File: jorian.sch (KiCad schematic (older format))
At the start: 101 parts, among them J1 USB-C, J2 USB-C, J3 MicroUSB, J4 MicroUSB, J5 MJ-4PP-9, Q1 AO3407, SW1 MSK-12C02, U1 E73-2G4M08S1C-52840, U2 E73-2G4M08S1C-52840, U3 MCP73831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

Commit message: updated files
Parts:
- removed H1: Battery Pad, kbd:battery_pad, symbol Mechanical:MountingHole_Pad
- removed JP1: +, kbd:jumper, symbol Device:Jumper_NO_Small
- removed JP10: -, kbd:jumper, symbol Device:Jumper_NO_Small
- removed JP16, JP25, JP26, JP27, JP28, JP29, JP30, JP31: (no value), kbd:jumper, symbol Device:Jumper_NO_Small
- removed OLED2: I2C_conn, kbd:connector_i2c, symbol Connector_Generic:Conn_01x04
- added Q2: SI2306, Package_TO_SOT_SMD:SOT-23, symbol Transistor_FET:BS870
- added R3: 10K, Resistor_SMD:R_0603_1608Metric, symbol Device:R
- JP11: symbol Connector_Generic:Conn_01x04 -> Connector_Generic:Conn_01x02
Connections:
- net labels added: LED_GND
- net labels removed: PGND
- wire segments 334 -> 317
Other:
- note added: "Power Control\nNormally On\nLow - Off\n"
- moved on the sheet: J5, U1, U2, X1

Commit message: updated files
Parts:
- removed J3, J4: MicroUSB, kbd:usb_micro_custom, symbol Connector:USB_B_Micro
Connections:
- no-connect marks 18 -> 14
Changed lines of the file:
@@
 	8000 9300 8500 9300
-$Comp
-L Connector:USB_B_Micro J3
-U 1 1 5DDAA442
-P 13125 5500
-F 0 "J3" H 13180 5967 50  0000 C CNN
-F 1 "MicroUSB" H 13180 5876 50  0000 C CNN
-F 2 "kbd:usb_micro_custom" H 13275 5450 50  0001 C CNN
-F 3 "~" H 13275 5450 50  0001 C CNN
-	1    13125 5500
-	1    0    0    -1
-$EndComp
-Text Label 13425 5300 0    50   ~ 0
-VUSB
-NoConn ~ 13025 5900
 $Comp
 L power:GND #PWR0108
@@
 Wire Wire Line
 	15125 5525 15125 5575
-NoConn ~ 13000 7125
-NoConn ~ 13400 6925
 NoConn ~ 14225 6525
 NoConn ~ 15125 6225
@@
 NoConn ~ 15125 5325
 NoConn ~ 15125 5225
-Text Label 13400 6525 0    50   ~ 0
-VUSB
-$Comp
-L Connector:USB_B_Micro J4
-U 1 1 5DDAA45A
-P 13100 6725
-F 0 "J4" H 13155 7192 50  0000 C CNN
-F 1 "MicroUSB" H 13155 7101 50  0000 C CNN
-F 2 "kbd:usb_micro_custom" H 13250 6675 50  0001 C CNN
-F 3 "~" H 13250 6675 50  0001 C CNN
-	1    13100 6725
-	1    0    0    -1
-$EndComp
 $Comp
 L jorian-rescue:USB_C_Receptacle_USB2.0-Connector J1
@@
 	1    0    0    -1
 $EndComp
-NoConn ~ 13425 5700
-$Comp
-L power:GND #PWR0109
-U 1 1 5DDAA46D
-P 13125 5900
-F 0 "#PWR0109" H 13125 5650 50  0001 C CNN
-F 1 "GND" H 13125 5750 50  0000 C CNN
-F 2 "" H 13125 5900 50  0001 C CNN
-F 3 "" H 13125 5900 50  0001 C CNN
-	1    13125 5900
-	-1   0    0    -1
-$EndComp
-$Comp
-L power:GND #PWR0112
-U 1 1 5DDAA473
-P 13100 7125
-F 0 "#PWR0112" H 13100 6875 50  0001 C CNN
-F 1 "GND" H 13100 6975 50  0000 C CNN
-F 2 "" H 13100 7125 50  0001 C CNN
-F 3 "" H 13100 7125 50  0001 C CNN
-	1    13100 7125
-	-1   0    0    -1
-$EndComp
 Text GLabel 15225 5575 2    50   Input ~ 0
 D-
@@
 Wire Wire Line
 	15125 5775 15225 5775
-Text GLabel 13425 5500 2    50   Input ~ 0
-D+
-Text GLabel 13425 5600 2    50   Input ~ 0
-D-
-Text GLabel 13400 6825 2    50   Input ~ 0
-D-
-Text GLabel 13400 6725 2    50   Input ~ 0
-D+
 Text GLabel 15125 5025 2    50   Input ~ 0
 VUSB

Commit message: updated files
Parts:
- removed JP18: LIPO+, kbd:jumper, symbol Device:Jumper_NO_Small
- removed JP19: LIPO-, kbd:jumper, symbol Device:Jumper_NO_Small
- removed JP20: BAT+, kbd:jumper, symbol Device:Jumper_NO_Small
- removed JP21: BAT-, kbd:jumper, symbol Device:Jumper_NO_Small
- added Q3: AO3407, Package_TO_SOT_SMD:SOT-23, symbol Transistor_FET:BSS83P
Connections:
- net labels added: LED_VCC
- net labels removed: LED_GND, LIPO+, LIPO-
- wire segments 317 -> 320
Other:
- moved on the sheet: BT1, C1, C2, C3, D1, D2, JP11, JP2, JP3, JP4, JP5, JP6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

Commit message: updated files
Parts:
- removed J2: USB-C, kbd:usb_type_c, symbol jorian-rescue:USB_C_Receptacle_USB2.0-Connector
- removed U2: E73-2G4M08S1C-52840, kbd:E73-2G4M08S1C-52840, symbol jorian-rescue:E73-2G4M08S1C-52840
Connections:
- net labels added: CC1, CC2
- wire segments 320 -> 303
- no-connect marks 14 -> 8
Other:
- moved on the sheet: R1, R2

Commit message: autorouted
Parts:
- removed JP11: SWD_conn, kbd:connector_swd, symbol Connector_Generic:Conn_01x02
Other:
- moved on the sheet: E10, E15, E16, E18, E19, E20, E21, E5, L18
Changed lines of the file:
@@
 L Connector_Generic:Conn_01x04 E16
 U 1 1 5C28A7CD
-P 10550 8100
-F 0 "E16" H 10550 8300 50  0000 C CNN
-F 1 "right" H 10550 7800 50  0000 C CNN
-F 2 "kbd:edge_conn" H 10550 8100 50  0001 C CNN
-F 3 "" H 10550 8100 50  0001 C CNN
-	1    10550 8100
+P 10300 7075
+F 0 "E16" H 10300 7275 50  0000 C CNN
+F 1 "right" H 10300 6775 50  0000 C CNN
+F 2 "kbd:edge_conn" H 10300 7075 50  0001 C CNN
+F 3 "" H 10300 7075 50  0001 C CNN
+	1    10300 7075
 	-1   0    0    -1
 $EndComp
@@
 L Connector_Generic:Conn_01x04 E18
 U 1 1 5C28AA80
-P 10350 8100
-F 0 "E18" H 10350 8300 50  0000 C CNN
-F 1 "left" H 10350 7800 50  0000 C CNN
-F 2 "kbd:edge_conn" H 10350 8100 50  0001 C CNN
-F 3 "" H 10350 8100 50  0001 C CNN
-	1    10350 8100
-	1    0    0    -1
-$EndComp
-Text Label 10750 8200 0    50   ~ 0
+P 10100 7075
+F 0 "E18" H 10100 7275 50  0000 C CNN
+F 1 "left" H 10100 6775 50  0000 C CNN
+F 2 "kbd:edge_conn" H 10100 7075 50  0001 C CNN
+F 3 "" H 10100 7075 50  0001 C CNN
+	1    10100 7075
+	1    0    0    -1
+$EndComp
+Text Label 10500 7175 0    50   ~ 0
 GND
-Text Label 10750 8300 0    50   ~ 0
+Text Label 10500 7275 0    50   ~ 0
 S18
-Text Label 10750 8000 0    50   ~ 0
+Text Label 10500 6975 0    50   ~ 0
 LED_VCC
 $Comp
 L Connector_Generic:Conn_01x04 E19
 U 1 1 5C6E087C
-P 10300 5250
-F 0 "E19" H 10300 5450 50  0000 C CNN
-F 1 "right" H 10300 4950 50  0000 C CNN
-F 2 "kbd:edge_conn" H 10300 5250 50  0001 C CNN
-F 3 "" H 10300 5250 50  0001 C CNN
-	1    10300 5250
+P 11800 5650
+F 0 "E19" H 11800 5850 50  0000 C CNN
+F 1 "right" H 11800 5350 50  0000 C CNN
+F 2 "kbd:edge_conn" H 11800 5650 50  0001 C CNN
+F 3 "" H 11800 5650 50  0001 C CNN
+	1    11800 5650
 	-1   0    0    -1
 $EndComp
@@
 L Connector_Generic:Conn_01x04 E5
 U 1 1 5C6E0883
-P 10100 5250
-F 0 "E5" H 10100 5450 50  0000 C CNN
-F 1 "left" H 10100 4950 50  0000 C CNN
-F 2 "kbd:edge_conn" H 10100 5250 50  0001 C CNN
-F 3 "" H 10100 5250 50  0001 C CNN
-	1    10100 5250
-	1    0    0    -1
-$EndComp
-Text Label 9900 5450 2    50   ~ 0
+P 11600 5650
+F 0 "E5" H 11600 5850 50  0000 C CNN
+F 1 "left" H 11600 5350 50  0000 C CNN
+F 2 "kbd:edge_conn" H 11600 5650 50  0001 C CNN
+F 3 "" H 11600 5650 50  0001 C CNN
+	1    11600 5650
+	1    0    0    -1
+$EndComp
+Text Label 11400 5850 2    50   ~ 0
 S19
-Text Label 9900 6150 2    50   ~ 0
+Text Label 11400 6550 2    50   ~ 0
 S20
 $Comp
 L Connector_Generic:Conn_01x04 E21
 U 1 1 5C6F2906
-P 10300 6650
-F 0 "E21" H 10300 6850 50  0000 C CNN
-F 1 "right" H 10300 6350 50  0000 C CNN
-F 2 "kbd:edge_conn" H 10300 6650 50  0001 C CNN
-F 3 "" H 10300 6650 50  0001 C CNN
-	1    10300 6650
+P 11800 7050
+F 0 "E21" H 11800 7250 50  0000 C CNN
+F 1 "right" H 11800 6750 50  0000 C CNN
+F 2 "kbd:edge_conn" H 11800 7050 50  0001 C CNN
+F 3 "" H 11800 7050 50  0001 C CNN
+	1    11800 7050
 	-1   0    0    -1
 $EndComp
@@
 L Connector_Generic:Conn_01x04 E15
 U 1 1 5C6F290D
-P 10100 6650
-F 0 "E15" H 10100 6850 50  0000 C CNN
-F 1 "left" H 10100 6350 50  0000 C CNN
-F 2 "kbd:edge_conn" H 10100 6650 50  0001 C CNN
-F 3 "" H 10100 6650 50  0001 C CNN
-	1    10100 6650
-	1    0    0    -1
-$EndComp
-Text Label 9900 5950 2    50   ~ 0
+P 11600 7050
+F 0 "E15" H 11600 7250 50  0000 C CNN
+F 1 "left" H 11600 6750 50  0000 C CNN
+F 2 "kbd:edge_conn" H 11600 7050 50  0001 C CNN
+F 3 "" H 11600 7050 50  0001 C CNN
+	1    11600 7050
+	1    0    0    -1
+$EndComp
+Text Label 11400 6350 2    50   ~ 0
 S22
-Text Label 10750 8100 0    50   ~ 0
+Text Label 10500 7075 0    50   ~ 0
 DIN18
-Text Label 10150 8300 2    50   ~ 0
+Text Label 9900 7275 2    50   ~ 0
 S18_A
-Text Label 10150 8200 2    50   ~ 0
+Text Label 9900 7175 2    50   ~ 0
 GND_A
-Text Label 10150 8000 2    50   ~ 0
+Text Label 9900 6975 2    50   ~ 0
 VCC_A
-Text Label 10150 8100 2    50   ~ 0
+Text Label 9900 7075 2    50   ~ 0
 DIN18_A
-Text Label 10500 5450 0    50   ~ 0
+Text Label 12000 5850 0    50   ~ 0
 S19_B
-Text Label 10500 6150 0    50   ~ 0
+Text Label 12000 6550 0    50   ~ 0
 S20_B
-Text Label 10500 6850 0    50   ~ 0
+Text Label 12000 7250 0    50   ~ 0
 S21_B
-Text Label 10500 5950 0    50   ~ 0
+Text Label 12000 6350 0    50   ~ 0
 S22_B
-Text Label 10500 6650 0    50   ~ 0
+Text Label 12000 7050 0    50   ~ 0
 VCC_B
-Text Label 10500 5250 0    50   ~ 0
+Text Label 12000 5650 0    50   ~ 0
 DIN21_B
-Text Label 9900 5150 2    50   ~ 0
+Text Label 11400 5550 2    50   ~ 0
 DIN5
-Text Label 10500 5150 0    50   ~ 0
+Text Label 12000 5550 0    50   ~ 0
 DIN5_B
-Text Label 9900 5250 2    50   ~ 0
+Text Label 11400 5650 2    50   ~ 0
 DIN21
 $Comp
@@
 L Connector_Generic:Conn_01x04 E20
 U 1 1 5C1C4E7E
-P 10300 5950
-F 0 "E20" H 10300 6150 50  0000 C CNN
-F 1 "right" H 10300 5650 50  0000 C CNN
-F 2 "kbd:edge_conn" H 10300 5950 50  0001 C CNN
-F 3 "" H 10300 5950 50  0001 C CNN
-	1    10300 5950
+P 11800 6350
+F 0 "E20" H 11800 6550 50  0000 C CNN
+F 1 "right" H 11800 6050 50  0000 C CNN
+F 2 "kbd:edge_conn" H 11800 6350 50  0001 C CNN
+F 3 "" H 11800 6350 50  0001 C CNN
+	1    11800 6350
 	-1   0    0    -1
 $EndComp
@@
 L Connector_Generic:Conn_01x04 E10
 U 1 1 5C1C4E85
-P 10100 5950
-F 0 "E10" H 10100 6150 50  0000 C CNN
-F 1 "left" H 10100 5650 50  0000 C CNN
-F 2 "kbd:edge_conn" H 10100 5950 50  0001 C CNN
-F 3 "" H 10100 5950 50  0001 C CNN
-	1    10100 5950
+P 11600 6350
+F 0 "E10" H 11600 6550 50  0000 C CNN
+F 1 "left" H 11600 6050 50  0000 C CNN
+F 2 "kbd:edge_conn" H 11600 6350 50  0001 C CNN
+F 3 "" H 11600 6350 50  0001 C CNN
+	1    11600 6350
 	1    0    0    -1
 $EndComp
@@
 L kbd:kbd_SK6812MINI L18
 U 1 1 5C54BB48
-P 9850 7375
-F 0 "L18" H 9850 7375 59  0000 C CNN
-F 1 "SK6812MINI" H 9850 7325 16  0000 C CNN
-F 2 "kbd:kbd_SK6812MINI" H 9850 7375 60  0001 C CNN
-F 3 "" H 9850 7375 60  0001 C CNN
-	1    9850 7375
+P 8175 7900
+F 0 "L18" H 8175 7900 59  0000 C CNN
+F 1 "SK6812MINI" H 8175 7850 16  0000 C CNN
+F 2 "kbd:kbd_SK6812MINI" H 8175 7900 60  0001 C CNN
+F 3 "" H 8175 7900 60  0001 C CNN
+	1    8175 7900
 	-1   0    0    -1
 $EndComp
-Text Label 9650 7275 2    50   ~ 0
+Text Label 7975 7800 2    50   ~ 0
 VCC_A
-Text Label 9650 7475 2    50   ~ 0
+Text Label 7975 8000 2    50   ~ 0
 DIN18_A
-Text Label 10050 7475 0    50   ~ 0
+Text Label 8375 8000 0    50   ~ 0
 GND_A
-NoConn ~ 10050 7275
+NoConn ~ 8375 7800
 Wire Wire Line
 	6100 3550 6100 4750
@@
 	0    -1   -1   0
 $EndComp
-Text GLabel 2500 1325 2    50   Input ~ 0
+Text GLabel 2500 2025 2    50   Input ~ 0
 S1
 $Comp
@@
 	1    0    0    -1
 $EndComp
-Text GLabel 2500 1225 2    50   Input ~ 0
+Text GLabel 2500 2125 2    50   Input ~ 0
 S2
-Text GLabel 2500 1125 2    50   Input ~ 0
+Text GLabel 2500 2225 2    50   Input ~ 0
 S3
 Text GLabel 1150 1925 0    50   Input ~ 0
@@
 Text GLabel 1150 1825 0    50   Input ~ 0
 S5
+Text GLabel 2500 1825 2    50   Input ~ 0
+S6
 Text GLabel 2500 1925 2    50   Input ~ 0
-S6
-Text GLabel 2500 1825 2    50   Input ~ 0
 S7
-Text GLabel 1150 2425 0    50   Input ~ 0
+Text GLabel 2500 2425 2    50   Input ~ 0
 S8
 Text GLabel 1150 1525 0    50   Input ~ 0
@@
 Text GLabel 1150 1325 0    50   Input ~ 0
 S10
-Text GLabel 1150 2625 0    50   Input ~ 0
+Text GLabel 2500 1425 2    50   Input ~ 0
 S11
-Text GLabel 2500 2025 2    50   Input ~ 0
+Text GLabel 2500 1625 2    50   Input ~ 0
 S12
 Text GLabel 1150 1025 0    50   Input ~ 0
 S13
-Text GLabel 2500 1425 2    50   Input ~ 0
+Text GLabel 1150 2625 0    50   Input ~ 0
 S14
-Text GLabel 2500 1625 2    50   Input ~ 0
+Text GLabel 1150 2425 0    50   Input ~ 0
 S15
-Text GLabel 2500 2125 2    50   Input ~ 0
+Text GLabel 2500 1225 2    50   Input ~ 0
 S16
-Text GLabel 2500 2225 2    50   Input ~ 0
+Text GLabel 2500 1325 2    50   Input ~ 0
 S17
-Text GLabel 2500 2425 2    50   Input ~ 0
+Text GLabel 2500 1125 2    50   Input ~ 0
 S18
 Text GLabel 1150 1725 0    50   Input ~ 0
@@
 Text GLabel 2500 2625 2    50   Input ~ 0
 RX
-Text Label 9900 6750 2    50   ~ 0
+Text Label 11400 7150 2    50   ~ 0
 GND
-Text Label 10500 6750 0    50   ~ 0
+Text Label 12000 7150 0    50   ~ 0
 GND_B
-Text Label 9900 6050 2    50   ~ 0
+Text Label 11400 6450 2    50   ~ 0
 GND
-Text Label 9900 6650 2    50   ~ 0
+Text Label 11400 7050 2    50   ~ 0
 LED_VCC
-Text Label 9900 6850 2    50   ~ 0
+Text Label 11400 7250 2    50   ~ 0
 S21
-Text Label 9900 5350 2    50   ~ 0
+Text Label 11400 5750 2    50   ~ 0
 GND
-Text Label 10500 5350 0    50   ~ 0
+Text Label 12000 5750 0    50   ~ 0
 GND_B
-NoConn ~ 10500 6550
-NoConn ~ 9900 6550
-NoConn ~ 9900 5850
-NoConn ~ 10500 5850
-Text Label 10500 6050 0    50   ~ 0
+NoConn ~ 12000 6950
+NoConn ~ 11400 6950
+NoConn ~ 11400 6250
+NoConn ~ 12000 6250
+Text Label 12000 6450 0    50   ~ 0
 GND_B
-Text GLabel 13225 5150 0    50   Input ~ 0
-SWC
-Text GLabel 13225 5250 0    50   Input ~ 0
-SWD
-$Comp
-L Connector_Generic:Conn_01x02 JP11
-U 1 1 5DDAA467
-P 13425 5150
-F 0 "JP11" H 13505 5192 50  0000 L CNN
-F 1 "SWD_conn" H 13505 5101 50  0000 L CNN
-F 2 "kbd:connector_swd" H 13425 5150 50  0001 C CNN
-F 3 "~" H 13425 5150 50  0001 C CNN
-	1    13425 5150
-	1    0    0    -1
-$EndComp
 $Comp
 L Transistor_FET:BS870 Q2

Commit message: better nr52 symbol, autorouted
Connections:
- net labels removed: P0.05, VDD
- wire segments 303 -> 301
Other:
- note added: "Physical layout:\n\n S1 S2 S3 S4 S5 S19\n\n S6 S7 S8 S9 S10 S20 S22\n\n S11 S12 S13 S14 S15 S21 \n\nS18 S16 S17 *"
- moved on the sheet: BT1, C1, C2, C3, D1, D2, J5, JP2, JP3, JP4, JP5, JP6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

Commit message: fully autorouted (leds are still on internal DCDC, not good)
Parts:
- added J2: USB-C, kbd:usb_type_c, symbol jorian-rescue:USB_C_Receptacle_USB2.0-Connector
- added SW2: MSK-12C02, kbd:switch_MSK-12C02_smd, symbol Switch:SW_SPDT
- added U2: E73-2G4M08S1C-52840, kbd:E73-2G4M08S1C-52840, symbol jorian-rescue:E73-2G4M08S1C-52840
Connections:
- net labels added: BAT_SW, PGND
- wire segments 301 -> 302
- no-connect marks 8 -> 12
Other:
- note added: "Top side layout:\n\n S1 S2 S3 S4 S5 S19\n\n S6 S7 S8 S9 S10 S20 S22\n\n S11 S12 S13 S14 S15 S21 \n\nS18 S16 S17 *"
- note added: "Underside layout:\n\n S19 S5 S4 S3 S2 S1\n\nS22 S20 S10 S9 S8 S7 S6\n\n S21 S15 S14 S13 S12 S11\n\n * S17 S16 S18\n"
- note added: "top underside pins"
- note removed: "Physical layout:\n\n S1 S2 S3 S4 S5 S19\n\n S6 S7 S8 S9 S10 S20 S22\n\n S11 S12 S13 S14 S15 S21 \n\nS18 S16 S17 *"
- note removed: "underside pins"
- moved on the sheet: C1, D2, J1, Q1, R1, R2, R5, R7, SW1

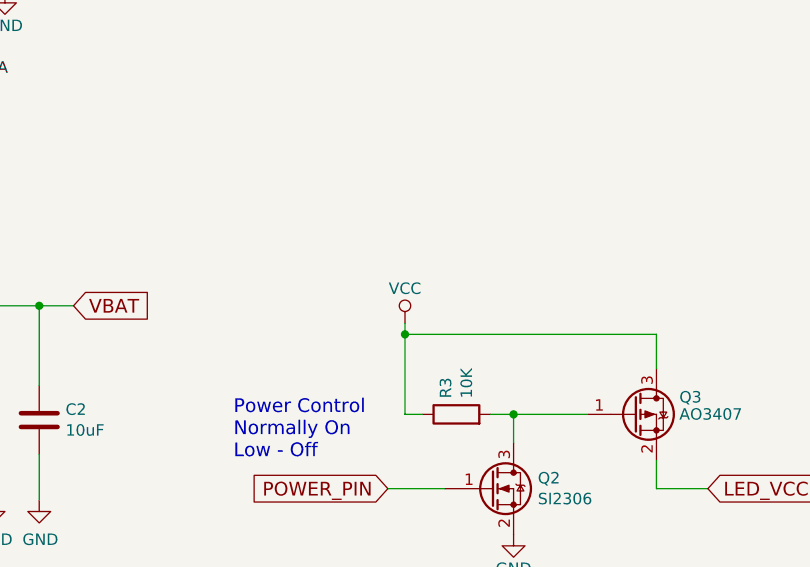
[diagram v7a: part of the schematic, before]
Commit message: LEDs power moved to to VDDH, autorouted
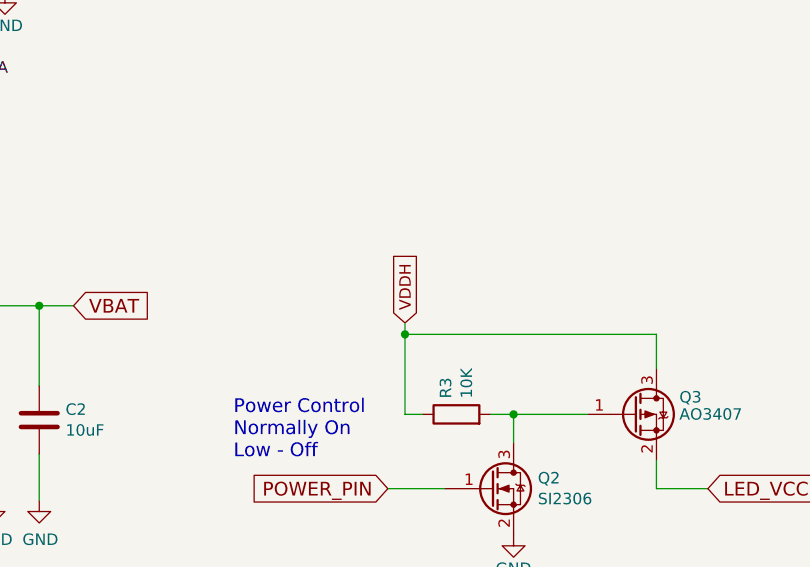
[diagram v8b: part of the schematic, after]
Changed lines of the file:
@@
 Power Control\nNormally On\nLow - Off\n
-$Comp
-L power:VCC #PWR0132
-U 1 1 5E6286BD
-P 10350 9075
-F 0 "#PWR0132" H 10350 8925 50  0001 C CNN
-F 1 "VCC" H 10350 9225 50  0000 C CNN
-F 2 "" H 10350 9075 50  0001 C CNN
-F 3 "" H 10350 9075 50  0001 C CNN
-	1    10350 9075
-	1    0    0    -1
-$EndComp
 $Comp
 L power:GND #PWR0133
@@
 NoConn ~ 3825 2250
 NoConn ~ 3975 2250
+Text GLabel 10350 9075 1    50   Input ~ 0
+VDDH
 $EndSCHEMATC
